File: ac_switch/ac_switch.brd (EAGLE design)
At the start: 34.3 x 79.8 mm, 23 parts, among them IC1 TINY85, T1 BC337

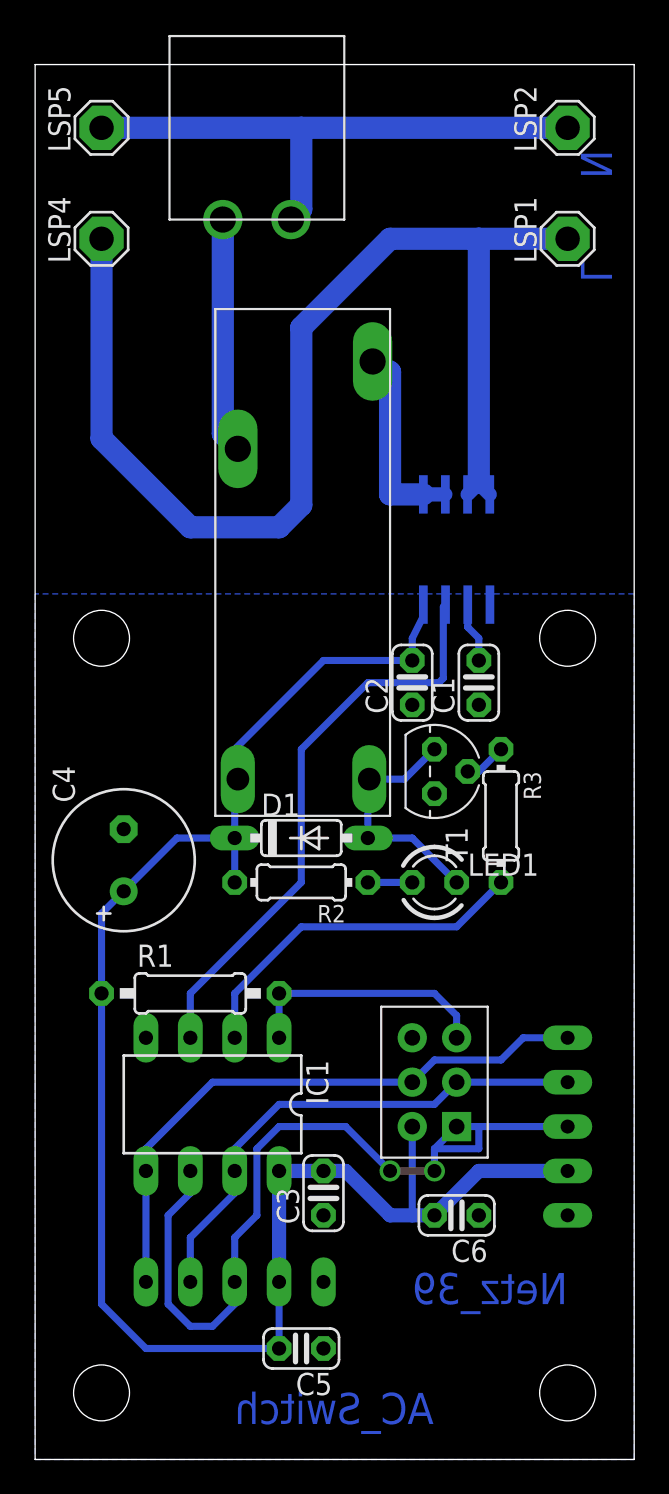
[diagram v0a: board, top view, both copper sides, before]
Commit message: Power-Board:  * Widerstands-Packages korrigiert  * Power-LED eingefügt
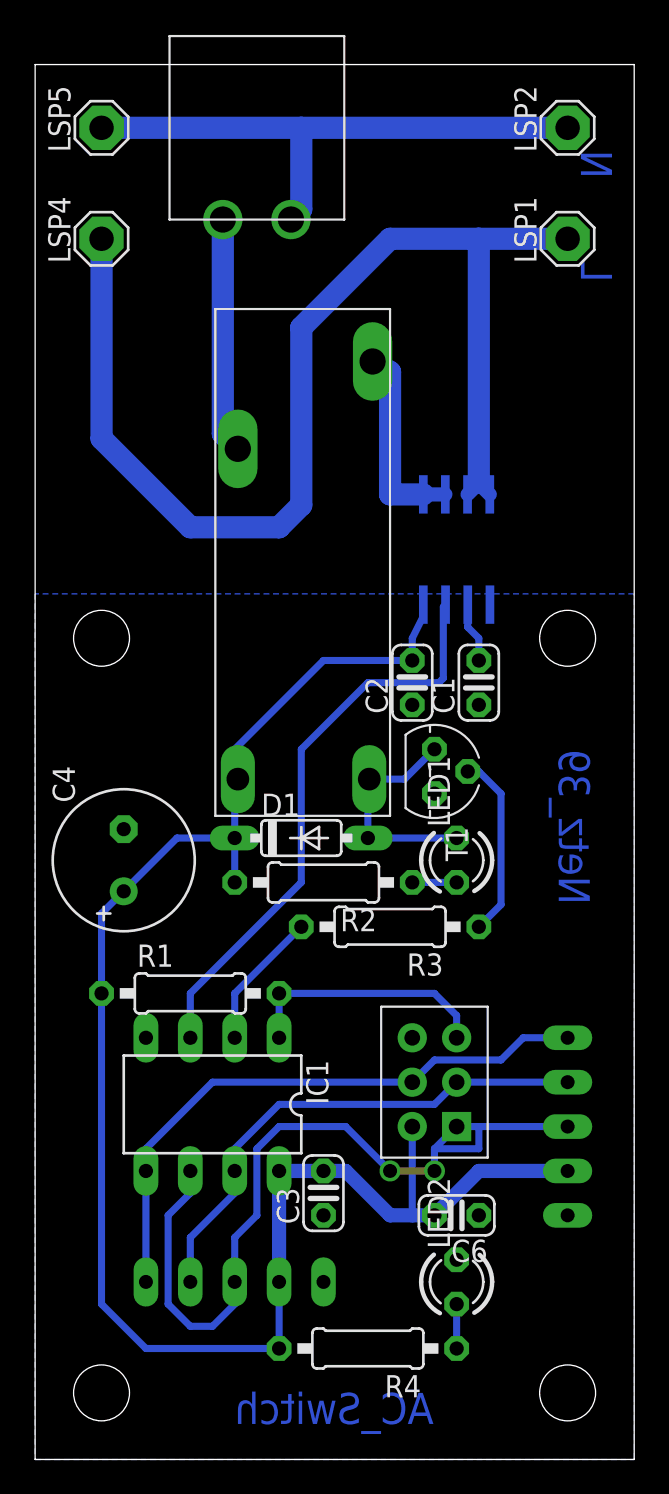
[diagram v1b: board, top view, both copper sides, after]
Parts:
- removed C5: 100n, resistor:C025-024X044
- added LED2: GN, led:LED3MM
- added R4: 220R, resistor:0207/10
- LED1: value (none) -> GE
- R2, R3: device resistor:0204/7 -> resistor:0207/10
- moved R3 8.98 mm to (20.3, 30.5), turned to 180 degrees
- moved LED1 1.80 mm to (24.1, 34.3), turned to 90 degrees
- moved R2 1.27 mm to (16.5, 33.0)
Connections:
- new net N$6: LED2.A, R4.1
- net GND: now also LED2.K; no longer C5.1
- net VCC: now also R4.2; no longer C5.2
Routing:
- net SWITCH: track 20.4 -> 7.93 mm
- net N$5: track 2.43 -> 10.6 mm
- net N$6: track 0.00 -> 2.54 mm
- net VCC: track 100.2 -> 101.5 mm
- net N$1: track 14.0 -> 12.9 mm
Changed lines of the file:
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@@
 <text x="33.02" y="74.93" size="1.778" layer="16" font="vector" rot="MR270">N</text>
 <text x="33.02" y="68.58" size="1.778" layer="16" font="vector" rot="MR270">L</text>
-<text x="30.48" y="8.89" size="1.778" layer="16" font="vector" rot="MR0">Netz_39</text>
+<text x="31.75" y="40.64" size="1.778" layer="16" font="vector" rot="MR270">Netz_39</text>
 <text x="11.43" y="3.81" size="1.778" layer="16" font="vector" rot="MR180">AC_Switch</text>
 <hole x="3.81" y="46.99" drill="3.2"/>
@@
 <element name="C3" library="resistor" package="C025-024X044" value="100n" x="16.51" y="15.24" rot="R90"/>
 <element name="R1" library="resistor" package="0207/10" value="10K" x="8.89" y="26.67"/>
-<element name="LED1" library="led" package="LED3MM" value="" x="22.86" y="33.02"/>
-<element name="R2" library="resistor" package="0204/7" value="220R" x="15.24" y="33.02" rot="R180"/>
+<element name="LED1" library="led" package="LED3MM" value="GE" x="24.13" y="34.29" rot="R90"/>
+<element name="R2" library="resistor" package="0207/10" value="220R" x="16.51" y="33.02" rot="R180"/>
 <element name="U$3" library="n39" package="I3C_PADS" value="I3C_PORT" x="11.43" y="10.16" rot="R270"/>
 <element name="U$4" library="n39" package="AVR_ISP" value="AVR_ISP" x="22.86" y="21.59" rot="R180"/>
@@
 <element name="C4" library="resistor" package="E3,5-8" value="68µ" x="5.08" y="34.29" rot="R90"/>
 <element name="U$5" library="n39" package="I3C_PADS" value="I3C_PORT" x="30.48" y="19.05" rot="R180"/>
-<element name="R3" library="resistor" package="0204/7" value="1,5K" x="26.67" y="36.83" rot="R270"/>
+<element name="R3" library="resistor" package="0207/10" value="1,5K" x="20.32" y="30.48" rot="R180"/>
 <element name="U$6" library="n39" package="WAGO_734_262" value="WAGO_734_262" x="12.7" y="76.2"/>
-<element name="C5" library="resistor" package="C025-024X044" value="100n" x="15.24" y="6.35" rot="R180"/>
 <element name="C6" library="resistor" package="C025-024X044" value="100n" x="24.13" y="13.97" rot="R180"/>
+<element name="LED2" library="led" package="LED3MM" value="GN" x="24.13" y="10.16" rot="R90"/>
+<element name="R4" library="resistor" package="0207/10" value="220R" x="19.05" y="6.35" rot="R180"/>
 </elements>
 <signals>
@@
 <vertex x="0" y="49.53"/>
 </polygon>
-<contactref element="C5" pad="1"/>
 <contactref element="C6" pad="1"/>
+<contactref element="LED2" pad="K"/>
 </signal>
 <signal name="VCC">
@@
 <wire x1="17.78" y1="16.51" x2="16.51" y2="16.51" width="0.8128" layer="16"/>
 <wire x1="13.97" y1="16.51" x2="13.97" y2="10.16" width="0.8128" layer="16"/>
-<wire x1="13.97" y1="10.16" x2="13.97" y2="6.35" width="0.4064" layer="16"/>
-<wire x1="13.97" y1="6.35" x2="6.35" y2="6.35" width="0.4064" layer="16"/>
 <wire x1="6.35" y1="6.35" x2="3.81" y2="8.89" width="0.4064" layer="16"/>
 <wire x1="3.81" y1="8.89" x2="3.81" y2="26.67" width="0.4064" layer="16"/>
@@
 <wire x1="3.81" y1="26.67" x2="3.81" y2="31.242" width="0.4064" layer="16"/>
 <wire x1="3.81" y1="31.242" x2="5.08" y2="32.512" width="0.4064" layer="16"/>
-<contactref element="C5" pad="2"/>
 <contactref element="C6" pad="2"/>
 <wire x1="22.86" y1="13.97" x2="25.4" y2="16.51" width="0.8128" layer="16"/>
 <wire x1="25.4" y1="16.51" x2="30.48" y2="16.51" width="0.8128" layer="16"/>
 <wire x1="21.59" y1="13.97" x2="22.86" y2="13.97" width="0.8128" layer="16"/>
+<wire x1="6.35" y1="6.35" x2="13.97" y2="6.35" width="0.4064" layer="16"/>
+<wire x1="13.97" y1="8.89" x2="13.97" y2="10.16" width="0.4064" layer="16"/>
+<contactref element="R4" pad="2"/>
+<wire x1="13.97" y1="6.35" x2="13.97" y2="10.16" width="0.4064" layer="16"/>
 </signal>
 <signal name="N$1">
@@
 <wire x1="22.86" y1="40.64" x2="21.15" y2="38.93" width="0.4064" layer="16"/>
 <wire x1="21.15" y1="38.93" x2="19.13" y2="38.93" width="0.4064" layer="16"/>
-<wire x1="24.13" y1="33.02" x2="21.59" y2="35.56" width="0.4064" layer="16"/>
-<wire x1="21.59" y1="35.56" x2="19.05" y2="35.56" width="0.4064" layer="16"/>
+<wire x1="24.13" y1="35.56" x2="19.05" y2="35.56" width="0.4064" layer="16"/>
 </signal>
 <signal name="N$2">
@@
 <wire x1="11.43" y1="24.13" x2="11.43" y2="26.67" width="0.4064" layer="16"/>
 <wire x1="11.43" y1="26.67" x2="15.24" y2="30.48" width="0.4064" layer="16"/>
-<wire x1="15.24" y1="30.48" x2="24.13" y2="30.48" width="0.4064" layer="16"/>
-<wire x1="24.13" y1="30.48" x2="26.67" y2="33.02" width="0.4064" layer="16"/>
 </signal>
 <signal name="SENSE">
@@
 <contactref element="R2" pad="1"/>
 <contactref element="LED1" pad="A"/>
-<wire x1="21.59" y1="33.02" x2="19.05" y2="33.02" width="0.4064" layer="16"/>
+<wire x1="24.13" y1="33.02" x2="21.59" y2="33.02" width="0.4064" layer="16"/>
 </signal>
 <signal name="N$5">
 <contactref element="T1" pad="2"/>
 <contactref element="R3" pad="1"/>
-<wire x1="26.67" y1="40.64" x2="25.4" y2="39.37" width="0.4064" layer="16"/>
+<wire x1="25.4" y1="30.48" x2="26.67" y2="31.75" width="0.4064" layer="16"/>
+<wire x1="26.67" y1="31.75" x2="26.67" y2="38.1" width="0.4064" layer="16"/>
+<wire x1="26.67" y1="38.1" x2="25.4" y2="39.37" width="0.4064" layer="16"/>
 <wire x1="25.4" y1="39.37" x2="24.765" y2="39.37" width="0.4064" layer="16"/>
 </signal>
+<signal name="N$6">
+<contactref element="R4" pad="1"/>
+<contactref element="LED2" pad="A"/>
+<wire x1="24.13" y1="8.89" x2="24.13" y2="6.35" width="0.4064" layer="16"/>
+</signal>
 </signals>
